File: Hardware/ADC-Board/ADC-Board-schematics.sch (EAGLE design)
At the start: 41 parts, among them U2 OPA2348AIDCNTG4

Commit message: Layout and parts
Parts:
- added C5: 10uF, rcl:CPOLRAD
- added U3: (no value), SparkFun-PowerIC:V_REG_LM1117SOT223
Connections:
- removed net 5VCON: JP1.1
- new net 5VDD: C27.1, C5.+, TLV71333.EN, TLV71333.IN, U3.OUT, U3.OUT@1
- new net 5VREF: C4.1, U2.V+
- net +12VDC: now also JP1.1, U3.IN
- net 5VCC: no longer C27.1, C4.1, TLV71333.EN, TLV71333.IN, U2.V+
- net GND: now also C5.-, U3.ADJ
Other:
- note added: "Audio reference voltage"
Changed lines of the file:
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@@
 <part name="POT1" library="SparkFun-Resistors" deviceset="TRIMPOT-PVZ2A" device=""/>
 <part name="POT2" library="SparkFun-Resistors" deviceset="TRIMPOT-PVZ2A" device=""/>
+<part name="U3" library="SparkFun-PowerIC" deviceset="V_REG_LM1117" device="SOT223">
+<attribute name="PROD_ID" value="VREG-08170"/>
+</part>
+<part name="GND2" library="supply1" deviceset="GND" device=""/>
+<part name="C5" library="rcl" deviceset="CPOLRAD" device="" value="10uF"/>
 </parts>
 <sheets>
@@
 <text x="-119.38" y="88.9" size="5.08" layer="91">Analog to digital conversion</text>
 <text x="-63.5" y="12.7" size="2.54" layer="91">Connector to RasPi</text>
+<text x="81.28" y="-73.66" size="1.778" layer="91">Audio reference voltage</text>
 </plain>
 <instances>
@@
 <instance part="POT1" gate="G$1" x="86.36" y="71.12" rot="R90"/>
 <instance part="POT2" gate="G$1" x="86.36" y="30.48" rot="R90"/>
+<instance part="U3" gate="G$1" x="93.98" y="-78.74"/>
+<instance part="GND2" gate="1" x="93.98" y="-93.98"/>
+<instance part="C5" gate="G$1" x="116.84" y="-83.82"/>
 </instances>
 <busses>
 </busses>
 <nets>
-<net name="5VCON" class="0">
-<segment>
-<pinref part="JP1" gate="A" pin="1"/>
-<wire x1="43.18" y1="-10.16" x2="30.48" y2="-10.16" width="0.1524" layer="91"/>
-<label x="27.94" y="-9.398" size="2.54" layer="95"/>
-</segment>
-</net>
 <net name="GND" class="0">
 <segment>
@@
 <pinref part="JP1" gate="A" pin="4"/>
 <pinref part="GND1" gate="1" pin="GND"/>
-<wire x1="50.8" y1="-12.7" x2="60.96" y2="-12.7" width="0.1524" layer="91"/>
+<wire x1="50.8" y1="-12.7" x2="55.88" y2="-12.7" width="0.1524" layer="91"/>
+<wire x1="55.88" y1="-12.7" x2="60.96" y2="-12.7" width="0.1524" layer="91"/>
 <wire x1="60.96" y1="-12.7" x2="60.96" y2="-20.32" width="0.1524" layer="91"/>
 <pinref part="JP1" gate="A" pin="2"/>
-<wire x1="50.8" y1="-12.7" x2="50.8" y2="-10.16" width="0.1524" layer="91"/>
-<junction x="50.8" y="-12.7"/>
+<wire x1="50.8" y1="-10.16" x2="55.88" y2="-10.16" width="0.1524" layer="91"/>
+<wire x1="55.88" y1="-10.16" x2="55.88" y2="-12.7" width="0.1524" layer="91"/>
+<junction x="55.88" y="-12.7"/>
 </segment>
 <segment>
@@
 <wire x1="142.24" y1="48.26" x2="142.24" y2="40.64" width="0.1524" layer="91"/>
 </segment>
+<segment>
+<pinref part="U3" gate="G$1" pin="ADJ"/>
+<pinref part="GND2" gate="1" pin="GND"/>
+<wire x1="93.98" y1="-86.36" x2="93.98" y2="-91.44" width="0.1524" layer="91"/>
+<pinref part="C5" gate="G$1" pin="-"/>
+<wire x1="116.84" y1="-88.9" x2="116.84" y2="-91.44" width="0.1524" layer="91"/>
+<wire x1="116.84" y1="-91.44" x2="93.98" y2="-91.44" width="0.1524" layer="91"/>
+<junction x="93.98" y="-91.44"/>
+</segment>
 </net>
 <net name="3V3" class="0">
@@
 <wire x1="66.04" y1="-38.1" x2="83.82" y2="-38.1" width="0.1524" layer="91"/>
 <label x="66.294" y="-36.83" size="2.54" layer="95"/>
+<wire x1="66.04" y1="-38.1" x2="55.88" y2="-38.1" width="0.1524" layer="91"/>
+<wire x1="55.88" y1="-38.1" x2="55.88" y2="-78.74" width="0.1524" layer="91"/>
+<junction x="66.04" y="-38.1"/>
+<pinref part="U3" gate="G$1" pin="IN"/>
+<wire x1="55.88" y1="-78.74" x2="86.36" y2="-78.74" width="0.1524" layer="91"/>
 </segment>
 <segment>
 <pinref part="JP1" gate="A" pin="3"/>
-<wire x1="43.18" y1="-12.7" x2="30.48" y2="-12.7" width="0.1524" layer="91"/>
+<wire x1="43.18" y1="-12.7" x2="38.1" y2="-12.7" width="0.1524" layer="91"/>
 <label x="26.67" y="-15.748" size="2.54" layer="95"/>
+<pinref part="JP1" gate="A" pin="1"/>
+<wire x1="38.1" y1="-12.7" x2="30.48" y2="-12.7" width="0.1524" layer="91"/>
+<wire x1="43.18" y1="-10.16" x2="38.1" y2="-10.16" width="0.1524" layer="91"/>
+<wire x1="38.1" y1="-10.16" x2="38.1" y2="-12.7" width="0.1524" layer="91"/>
+<junction x="38.1" y="-12.7"/>
 </segment>
 </net>
@@
 </segment>
 <segment>
-<wire x1="-30.48" y1="-35.56" x2="-38.1" y2="-35.56" width="0.1524" layer="91"/>
-<label x="-53.34" y="-35.56" size="2.54" layer="95"/>
-<pinref part="C27" gate="G$1" pin="1"/>
-<wire x1="-38.1" y1="-35.56" x2="-50.8" y2="-35.56" width="0.1524" layer="91"/>
-<wire x1="-50.8" y1="-35.56" x2="-53.34" y2="-35.56" width="0.1524" layer="91"/>
-<wire x1="-50.8" y1="-35.56" x2="-50.8" y2="-38.1" width="0.1524" layer="91"/>
-<junction x="-50.8" y="-35.56"/>
-<wire x1="-30.48" y1="-45.72" x2="-38.1" y2="-45.72" width="0.1524" layer="91"/>
-<wire x1="-38.1" y1="-45.72" x2="-38.1" y2="-35.56" width="0.1524" layer="91"/>
-<junction x="-38.1" y="-35.56"/>
-<pinref part="TLV71333" gate="G$1" pin="IN"/>
-<pinref part="TLV71333" gate="G$1" pin="EN"/>
-</segment>
-<segment>
 <pinref part="R4" gate="G$1" pin="2"/>
-<wire x1="55.88" y1="86.36" x2="55.88" y2="88.9" width="0.1524" layer="91"/>
-<wire x1="55.88" y1="88.9" x2="60.96" y2="88.9" width="0.1524" layer="91"/>
-<label x="55.88" y="88.9" size="1.778" layer="95"/>
+<wire x1="55.88" y1="86.36" x2="55.88" y2="91.44" width="0.1524" layer="91"/>
+<wire x1="55.88" y1="91.44" x2="60.96" y2="91.44" width="0.1524" layer="91"/>
 </segment>
 <segment>
 <pinref part="R8" gate="G$1" pin="1"/>
-<wire x1="55.88" y1="43.18" x2="55.88" y2="45.72" width="0.1524" layer="91"/>
-<wire x1="55.88" y1="45.72" x2="60.96" y2="45.72" width="0.1524" layer="91"/>
-<label x="55.88" y="45.72" size="1.778" layer="95"/>
-</segment>
-<segment>
-<pinref part="U2" gate="A" pin="V+"/>
-<wire x1="33.02" y1="43.18" x2="43.18" y2="43.18" width="0.1524" layer="91"/>
-<pinref part="C4" gate="G$1" pin="1"/>
-<wire x1="43.18" y1="43.18" x2="43.18" y2="38.1" width="0.1524" layer="91"/>
-<label x="38.1" y="43.18" size="1.778" layer="95"/>
+<wire x1="55.88" y1="43.18" x2="55.88" y2="48.26" width="0.1524" layer="91"/>
+<wire x1="55.88" y1="48.26" x2="60.96" y2="48.26" width="0.1524" layer="91"/>
 </segment>
 </net>
@@
 </segment>
 </net>
+<net name="5VREF" class="0">
+<segment>
+<pinref part="C4" gate="G$1" pin="1"/>
+<wire x1="43.18" y1="38.1" x2="43.18" y2="43.18" width="0.1524" layer="91"/>
+<pinref part="U2" gate="A" pin="V+"/>
+<wire x1="43.18" y1="43.18" x2="33.02" y2="43.18" width="0.1524" layer="91"/>
+<label x="36.322" y="43.688" size="2.54" layer="95"/>
+</segment>
+</net>
+<net name="5VDD" class="0">
+<segment>
+<pinref part="TLV71333" gate="G$1" pin="EN"/>
+<wire x1="-30.48" y1="-45.72" x2="-38.1" y2="-45.72" width="0.1524" layer="91"/>
+<wire x1="-38.1" y1="-45.72" x2="-38.1" y2="-35.56" width="0.1524" layer="91"/>
+<pinref part="TLV71333" gate="G$1" pin="IN"/>
+<wire x1="-38.1" y1="-35.56" x2="-30.48" y2="-35.56" width="0.1524" layer="91"/>
+<pinref part="C27" gate="G$1" pin="1"/>
+<wire x1="-38.1" y1="-35.56" x2="-50.8" y2="-35.56" width="0.1524" layer="91"/>
+<wire x1="-50.8" y1="-35.56" x2="-50.8" y2="-38.1" width="0.1524" layer="91"/>
+<junction x="-38.1" y="-35.56"/>
+<label x="-50.8" y="-33.02" size="2.54" layer="95"/>
+</segment>
+<segment>
+<pinref part="U3" gate="G$1" pin="OUT@1"/>
+<wire x1="101.6" y1="-81.28" x2="106.68" y2="-81.28" width="0.1524" layer="91"/>
+<wire x1="106.68" y1="-81.28" x2="106.68" y2="-78.74" width="0.1524" layer="91"/>
+<pinref part="U3" gate="G$1" pin="OUT"/>
+<wire x1="106.68" y1="-78.74" x2="101.6" y2="-78.74" width="0.1524" layer="91"/>
+<pinref part="C5" gate="G$1" pin="+"/>
+<wire x1="116.84" y1="-78.74" x2="116.84" y2="-81.28" width="0.1524" layer="91"/>
+<wire x1="106.68" y1="-78.74" x2="116.84" y2="-78.74" width="0.1524" layer="91"/>
+<junction x="106.68" y="-78.74"/>
+<label x="109.22" y="-76.2" size="2.54" layer="95"/>
+</segment>
+</net>

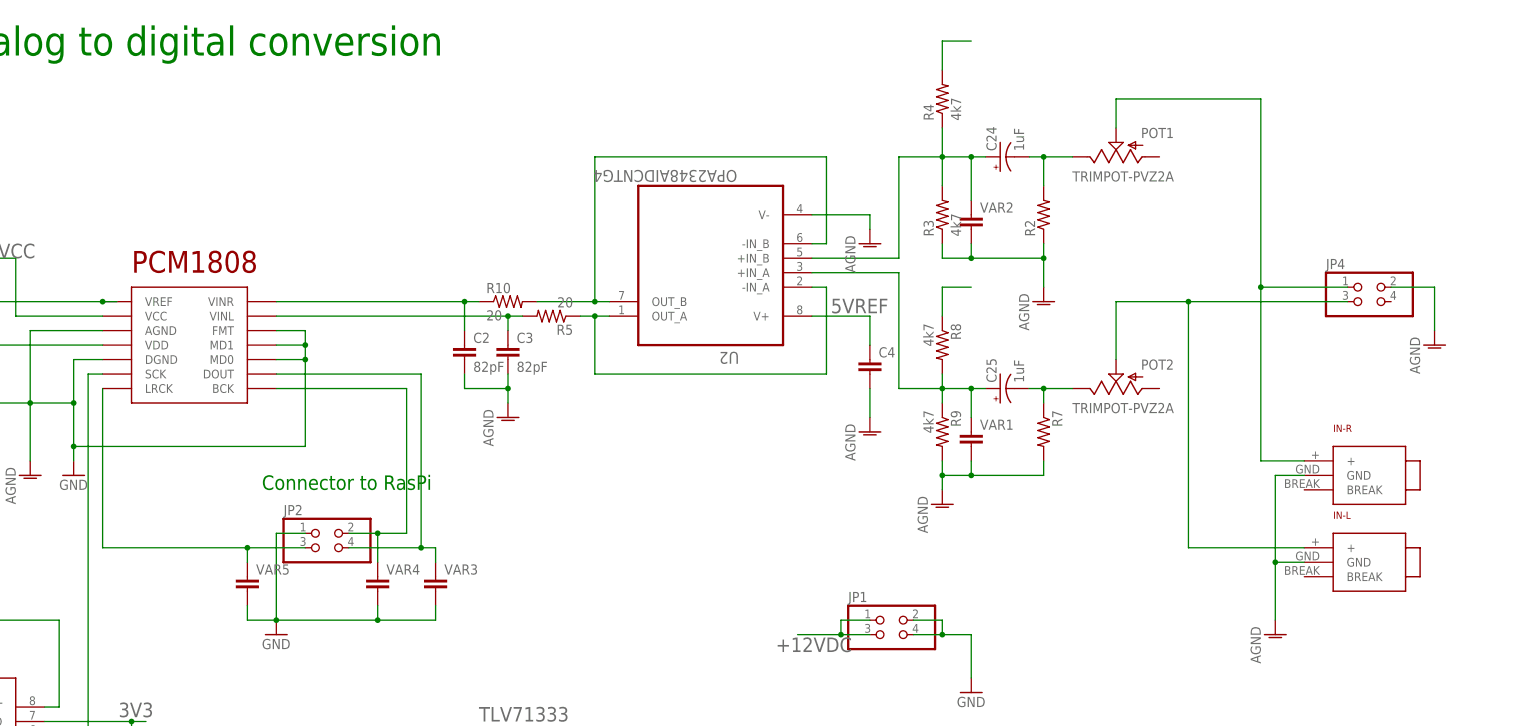
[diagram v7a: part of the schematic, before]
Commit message: ADC-board layout
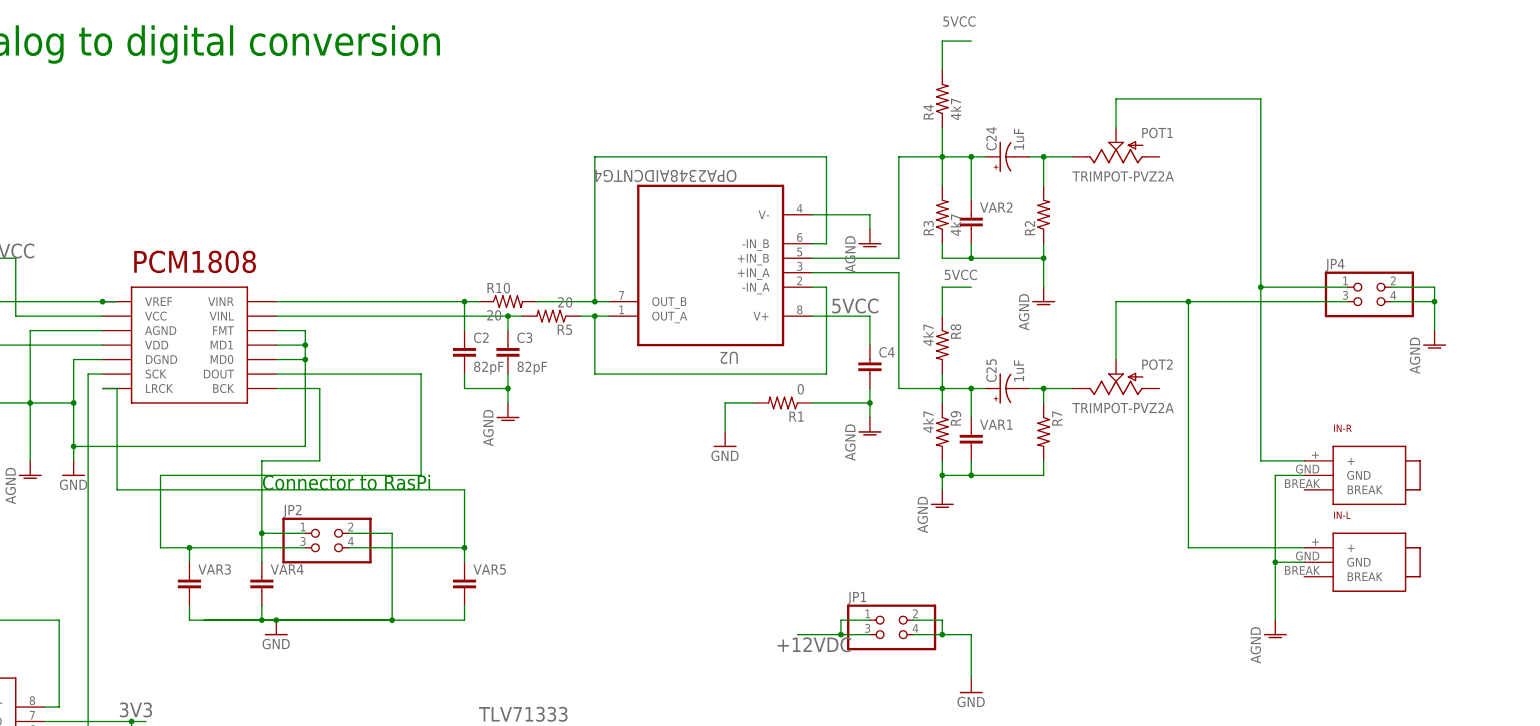
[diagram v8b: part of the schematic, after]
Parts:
- added R1: 0, SparkFun-Passives:RESISTOR0603-RES
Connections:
- removed net 5VREF: C4.1, U2.V+
- removed net N$2: JP2.3, PCM1808.LRCK, VAR5.1
- new net N$12: JP2.4, PCM1808.LRCK, VAR5.1
- net 5VCC: now also C4.1, U2.V+
- net AGND: now also JP4.2, JP4.4, R1.1
- net GND: now also JP2.2, R1.2; no longer JP2.1, JP4.2
- net N$1: now also JP2.1; no longer JP2.2
- net N$4: now also JP2.3; no longer JP2.4
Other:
- moved on the sheet: VAR3, VAR4, VAR5
